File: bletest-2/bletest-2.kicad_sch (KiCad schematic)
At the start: 6 parts, among them Y1 Crystal

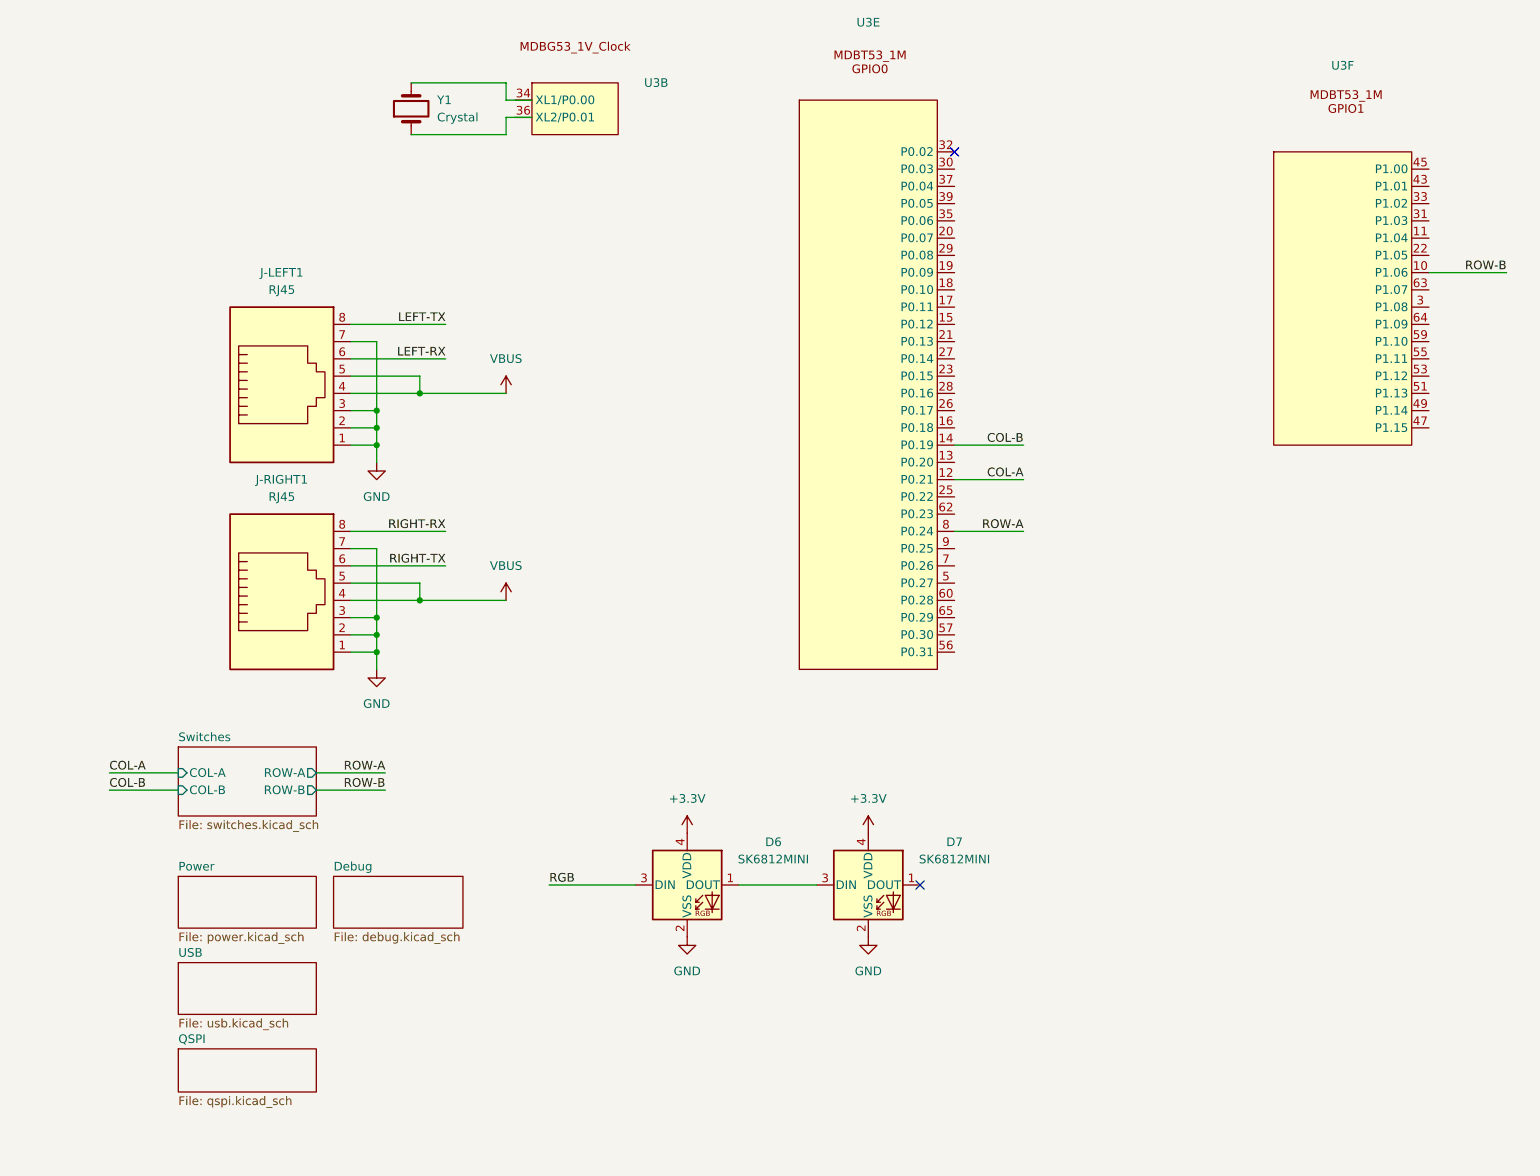
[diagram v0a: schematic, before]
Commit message: Full routing done
There are still a bunch of ERC violations.
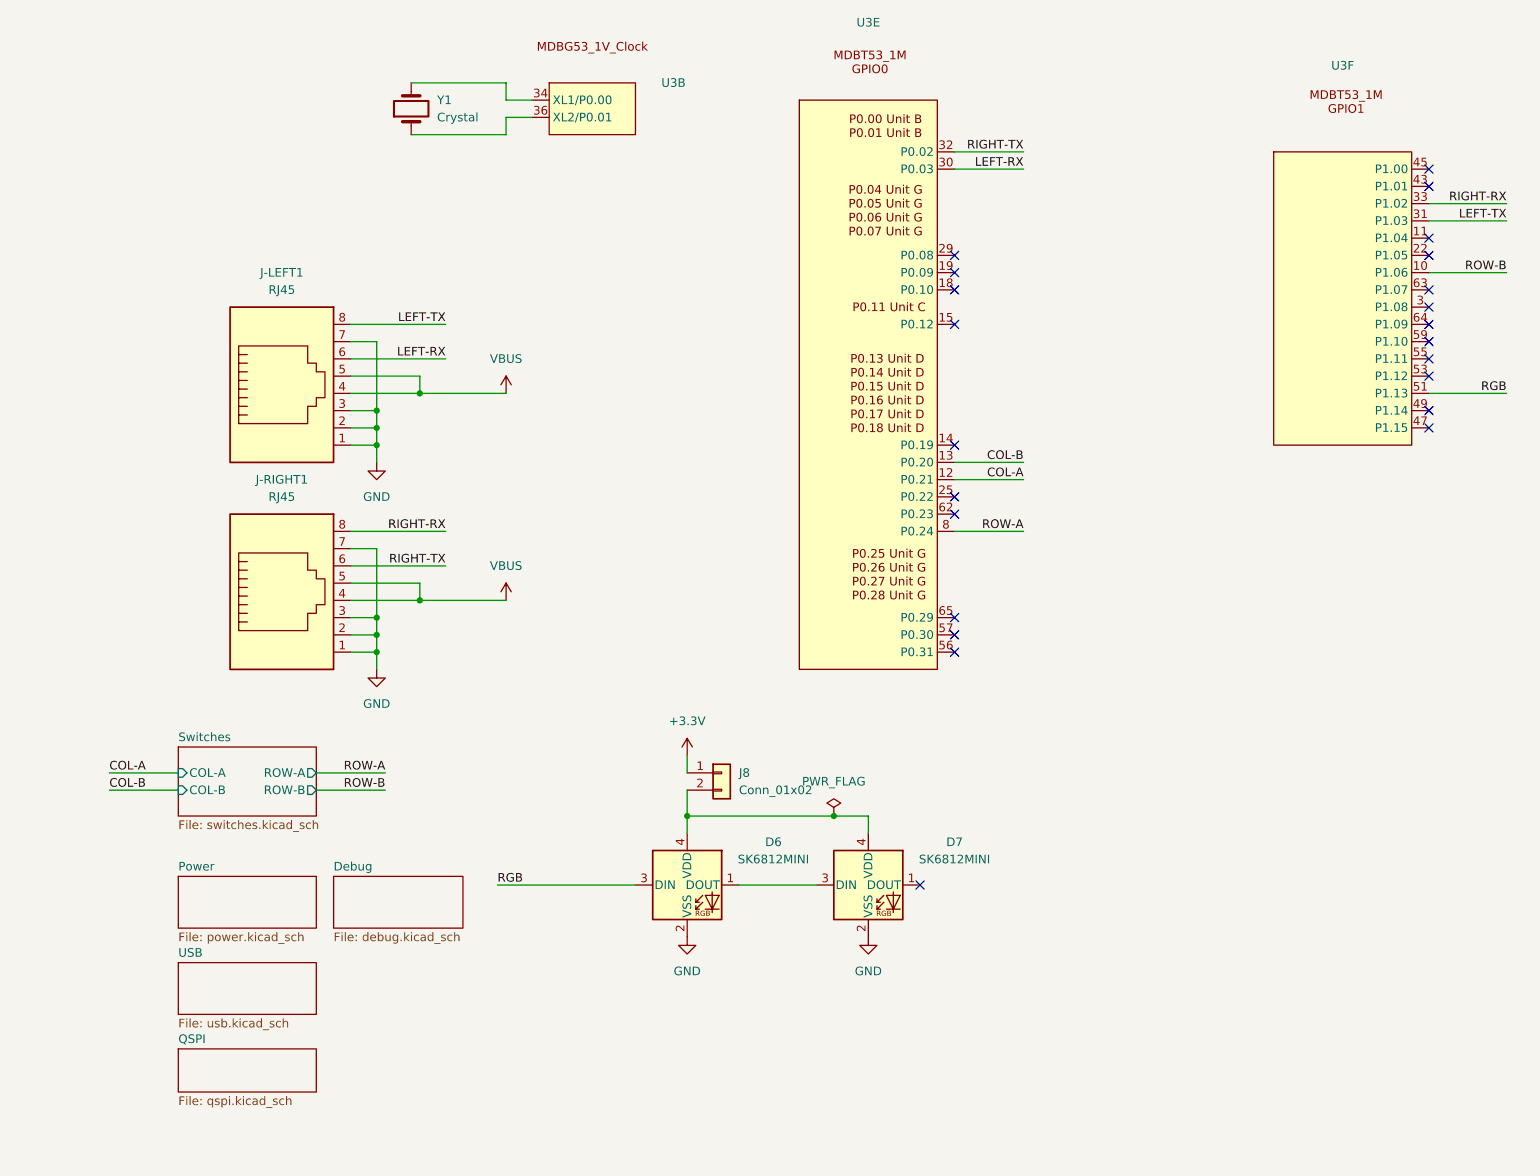
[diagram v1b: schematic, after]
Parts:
- added J8: Conn_01x02, Connector_PinHeader_2.54mm:PinHeader_1x02_P2.54mm_Vertical, symbol Connector_Generic:Conn_01x02
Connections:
- net +3.3V: now also J8.1 (Pin_1); no longer D6.4 (VDD), D7.4 (VDD)
- net COL-B: now also U3.13 (P0.20); no longer U3.14 (P0.19)
- net LEFT-RX: now also U3.30 (P0.03)
- net LEFT-TX: now also U3.31 (P1.03)
- net RGB: now also U3.51 (P1.13)
- net RIGHT-RX: now also U3.33 (P1.02)
- net RIGHT-TX: now also U3.32 (P0.02)
- net at U3.34 (XL1/P0.00): now also Y1.2
- net at U3.36 (XL2/P0.01): now also Y1.1
- new net: D6.4 (VDD), D7.4 (VDD), J8.2 (Pin_2)
- no-connect marks 2 -> 23
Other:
- moved on the sheet: U3B

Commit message: Rev A of bletest
Finish cleanup, and remove last remaining violations.

There are a handful of silkscreen overlaps with explicit exclusions.
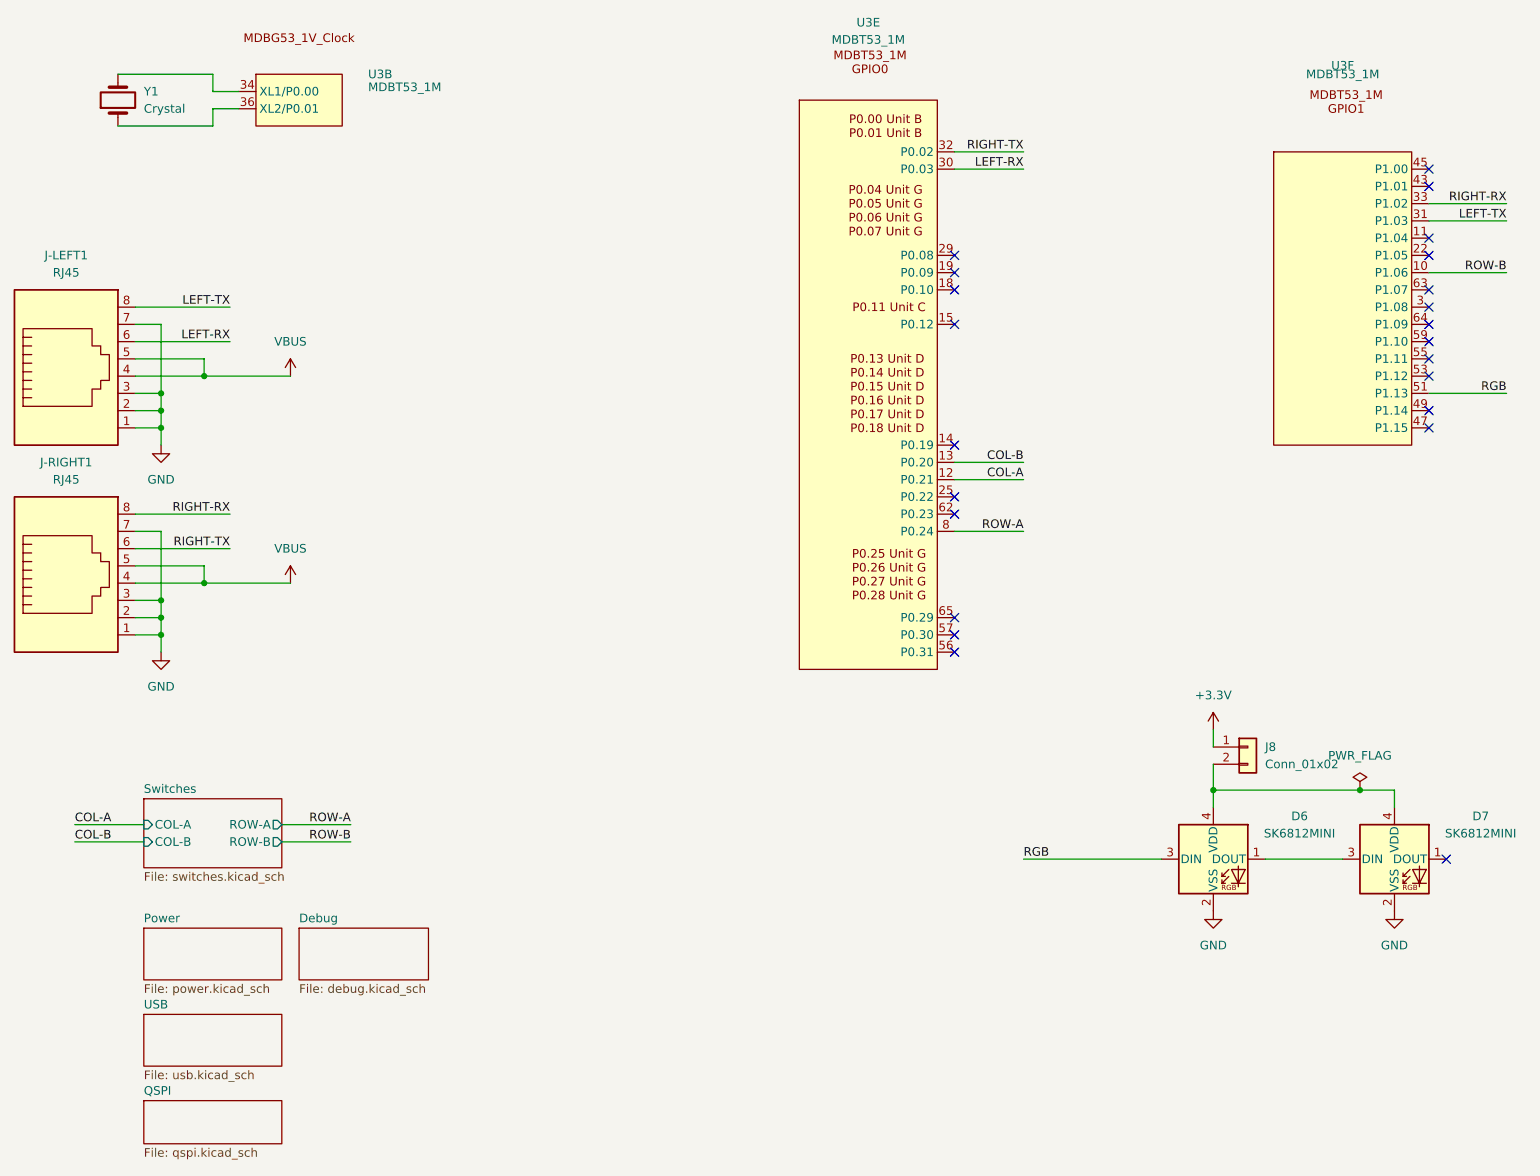
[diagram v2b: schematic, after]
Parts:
- U3: value ~ -> MDBT53_1M
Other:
- company: (none) -> David Brown
- title: (none) -> BLETEXT-2
- moved on the sheet: D6, D7, J-LEFT1, J-RIGHT1, J8, U3B, Y1
